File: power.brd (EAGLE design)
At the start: 186 x 186 mm, 126 parts, among them CN2 2X10 HEADER, Q1 IXTK180N15P, Q2 IXTK180N15P, Q4 SPD15P10PL, Q5 2N7002, U1 LT1630, U10 LM2936, U11 LM317, U12 SPST SSR, U2 LT1630, U3 DCDC 15V, U4 DAC80501, U5 DAC80501, U6 ADS1120, U7 LM2662, U8 LM7805, U9 TPS3700

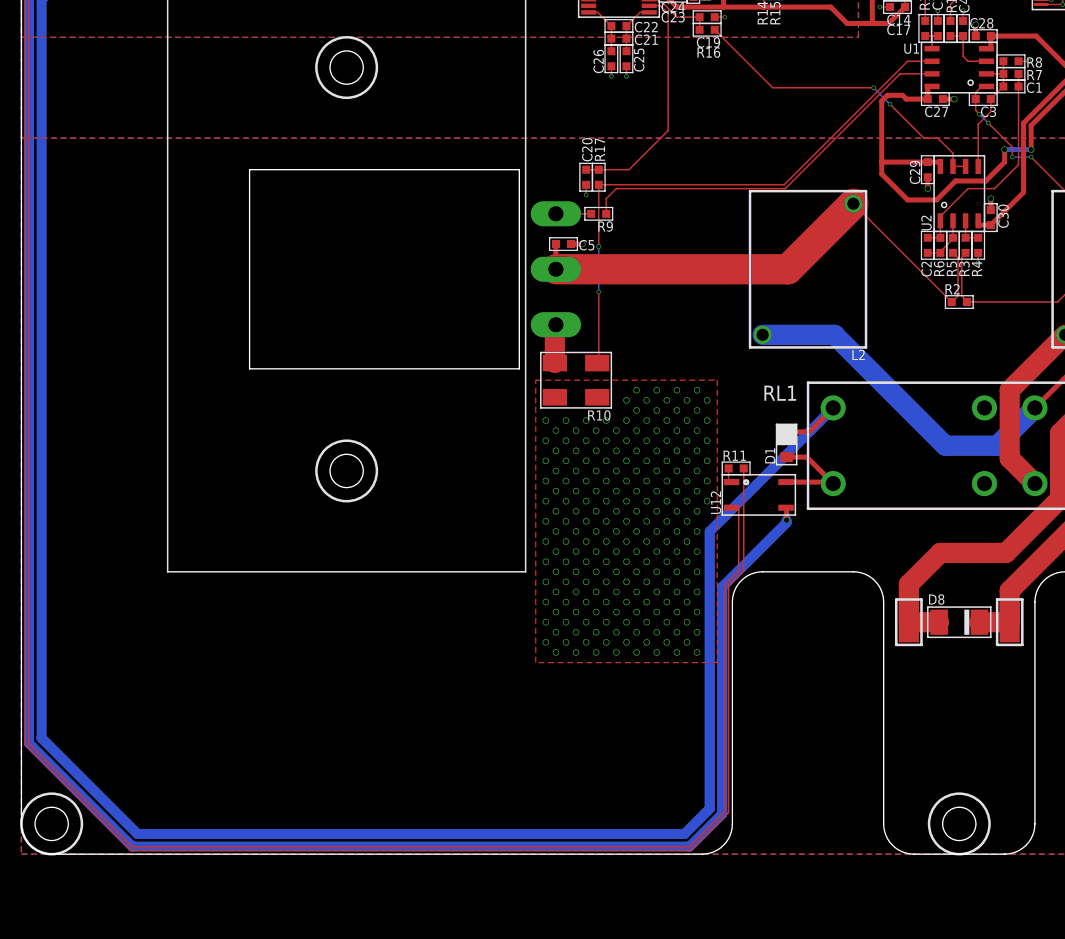
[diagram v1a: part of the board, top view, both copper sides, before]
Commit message: Fixes for stability
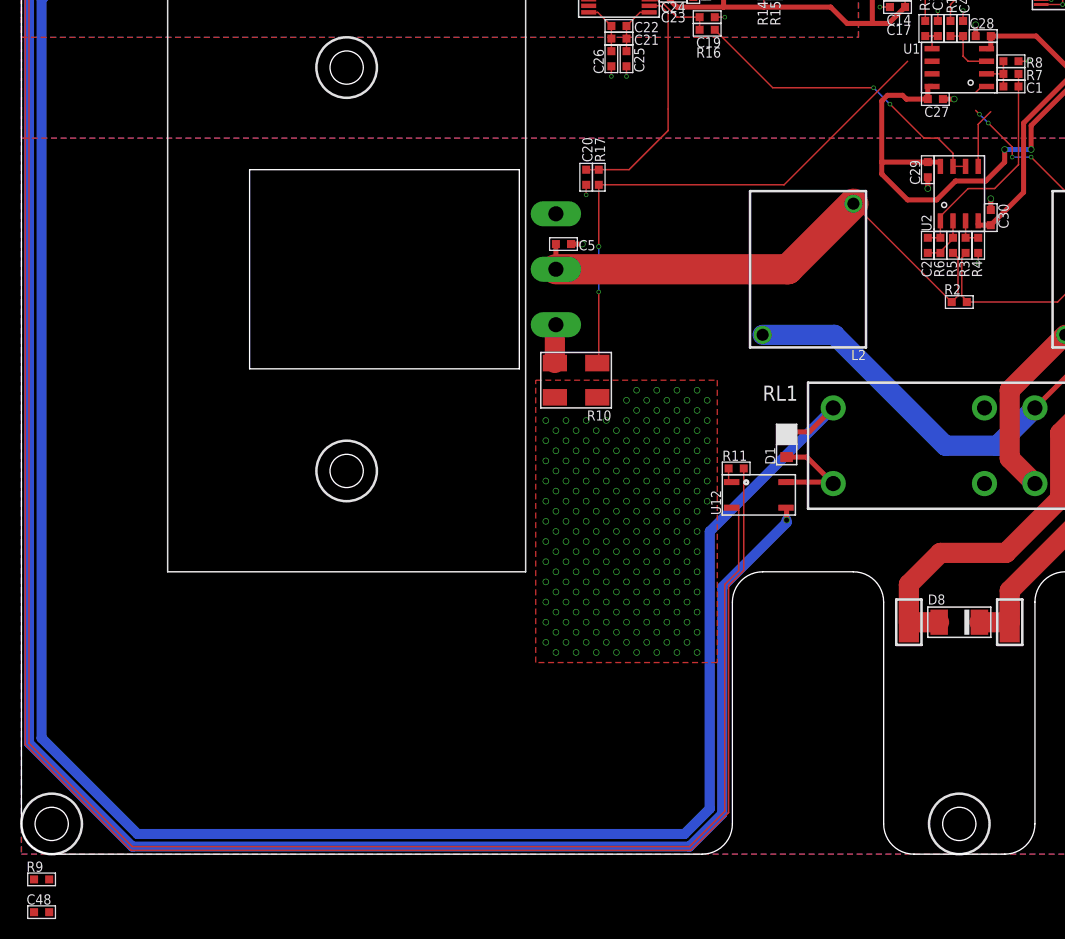
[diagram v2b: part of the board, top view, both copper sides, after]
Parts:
- removed C3: 220pF 50V, CAPACITORS:0603
- added C48: 330pF 50V, CAPACITORS:0603
- C5: value 100nF 16V -> 47nF 16V
- R9: value 10R -> 110R
- moved R9 86.1 mm to (-91.0, -95.5), turned to 0 degrees
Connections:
- net N$1: no longer C3.2
- net N$11: now also C48.1, R9.1, U1.6; no longer Q2.1, R9.2
- net N$345: no longer C3.1
- net N$76: now also R9.2; no longer U1.6
- net N$9: now also C48.2, Q2.1; no longer R9.1
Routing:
- net N$9: track 38.9 -> 0.00 mm
- net N$11: track 3.50 -> 0.00 mm
- net N$345: track 13.1 -> 10.1 mm
- net N$76: track 55.9 -> 53.4 mm
- net N$1: track 45.9 -> 44.1 mm
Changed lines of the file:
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@@
 <attribute name="PRICE_PER" value="0.14" x="89.585" y="16.785" size="1.778" layer="27" rot="R90" display="off"/>
-</element>
-<element name="C3" library="CAPACITORS" package="0603" value="220pF 50V" x="2.375" y="-18.125" smashed="yes" rot="R180">
-<attribute name="DIGIKEY" value="311-1073-1-ND" x="-73.825" y="78.395" size="1.778" layer="27" rot="R180" display="off"/>
-<attribute name="HEIGHT" value="1" x="-73.825" y="78.395" size="1.778" layer="27" rot="R180" display="off"/>
-<attribute name="NAME" x="3.75" y="-18.875" size="1.016" layer="25" rot="R180"/>
-<attribute name="PRICE_PER" value="0.08" x="-73.825" y="78.395" size="1.778" layer="27" rot="R180" display="off"/>
 </element>
 <element name="C30" library="CAPACITORS" package="0603" value="100nF 16V" x="3.125" y="-29.875" smashed="yes" rot="R90">
@@
 <attribute name="PRICE_PER" value="0.08" x="-67.96" y="-53.76" size="1.778" layer="27" rot="R270" display="off"/>
 </element>
-<element name="C5" library="CAPACITORS" package="0603" value="100nF 16V" x="-39.25" y="-32.5" smashed="yes">
-<attribute name="DIGIKEY" value="1276-6582-1-ND" x="44.57" y="-129.02" size="1.778" layer="27" display="off"/>
+<element name="C5" library="CAPACITORS" package="0603" value="47nF 16V" x="-39.25" y="-32.5" smashed="yes">
+<attribute name="DIGIKEY" value="1276-2079-1-ND" x="44.57" y="-129.02" size="1.778" layer="27" display="off"/>
 <attribute name="HEIGHT" value="1" x="44.57" y="-129.02" size="1.778" layer="27" display="off"/>
 <attribute name="NAME" x="-37.75" y="-33.125" size="1.016" layer="25"/>
@@
 <attribute name="NAME" x="6.625" y="-15" size="1.016" layer="25"/>
 <attribute name="PRICE_PER" value="0.10000" x="-40.595" y="85.955" size="1.778" layer="27" rot="R180" display="off"/>
-</element>
-<element name="R9" library="r_0603" package="0603" value="10R" x="-35.75" y="-29.5" smashed="yes" rot="R180">
-<attribute name="DIGIKEY" value="P10.0HCT-ND" x="-85.28" y="70.83" size="1.778" layer="27" rot="R180" display="off"/>
-<attribute name="FARNELL" value="" x="-85.28" y="70.83" size="1.778" layer="27" rot="R180" display="off"/>
-<attribute name="NAME" x="-34.25" y="-30.25" size="1.016" layer="25" rot="R180"/>
-<attribute name="PRICE_PER" value="0.10000" x="-85.28" y="70.83" size="1.778" layer="27" rot="R180" display="off"/>
 </element>
 <element name="RL1" library="ELECTROMECH" package="30MMDPDTRELAY" value="RT424012" x="0" y="-52.5" smashed="yes">
@@
 <attribute name="PRICE_PER" value="0.10000" x="-22.125" y="-54.75" size="1.778" layer="27" rot="R180" display="off"/>
 </element>
+<element name="R9" library="r_0603" package="0603" value="110R" x="-91" y="-95.5" smashed="yes">
+<attribute name="DIGIKEY" value="P110HCT-ND" x="-91" y="-95.5" size="1.778" layer="27" display="off"/>
+<attribute name="FARNELL" value="" x="-91" y="-95.5" size="1.778" layer="27" display="off"/>
+<attribute name="NAME" x="-92.5" y="-94.75" size="1.016" layer="25"/>
+<attribute name="PRICE_PER" value="0.10000" x="-91" y="-95.5" size="1.778" layer="27" display="off"/>
+</element>
+<element name="C48" library="CAPACITORS" package="0603" value="330pF 50V" x="-91" y="-98.75" smashed="yes">
+<attribute name="DIGIKEY" value="311-1075-1-ND" x="-91" y="-98.75" size="1.778" layer="27" display="off"/>
+<attribute name="HEIGHT" value="1" x="-91" y="-98.75" size="1.778" layer="27" display="off"/>
+<attribute name="NAME" x="-92.5" y="-98" size="1.016" layer="25"/>
+<attribute name="PRICE_PER" value="0.1" x="-91" y="-98.75" size="1.778" layer="27" display="off"/>
+</element>
 </elements>
 <signals>
 <signal name="N$1">
 <contactref element="R1" pad="1"/>
-<contactref element="C3" pad="2"/>
 <contactref element="U1" pad="1"/>
 <via x="2" y="-19.625" extent="1-16" drill="0.3"/>
@@
 <wire x1="16" y1="-32.75" x2="23.75" y2="-40.5" width="0.15" layer="1"/>
 <wire x1="23.75" y1="-40.5" x2="35" y2="-40.5" width="0.15" layer="1"/>
-<wire x1="1.625" y1="-18.125" x2="1.625" y2="-19.25" width="0.15" layer="1"/>
 <wire x1="1.625" y1="-19.25" x2="2" y2="-19.625" width="0.15" layer="1"/>
 <wire x1="2.7" y1="-16.875" x2="2.22" y2="-16.875" width="0.15" layer="1"/>
 <wire x1="2.22" y1="-16.875" x2="1.625" y2="-17.47" width="0.15" layer="1"/>
-<wire x1="1.625" y1="-17.47" x2="1.625" y2="-18.125" width="0.15" layer="1"/>
+<wire x1="1.625" y1="-19.25" x2="1.625" y2="-17.47" width="0" layer="19" extent="1-1"/>
 </signal>
 <signal name="N$2">
@@
 <wire x1="-0.875" y1="-11.875" x2="0.375" y2="-11.875" width="0.15" layer="1"/>
 </signal>
-<signal name="N$9">
-<contactref element="R9" pad="1"/>
-<contactref element="U1" pad="7"/>
-<wire x1="-35" y1="-29.5" x2="-35" y2="-28" width="0.15" layer="1"/>
-<wire x1="-34" y1="-27" x2="-35" y2="-28" width="0.15" layer="1"/>
-<wire x1="-17.25" y1="-27" x2="-34" y2="-27" width="0.15" layer="1"/>
-<wire x1="-5.875" y1="-15.625" x2="-2.7" y2="-15.625" width="0.15" layer="1"/>
-<wire x1="-17.25" y1="-27" x2="-5.875" y2="-15.625" width="0.15" layer="1"/>
-</signal>
-<signal name="N$11">
-<contactref element="R9" pad="2"/>
-<contactref element="Q2" pad="1"/>
-<wire x1="-40" y1="-29.5" x2="-36.5" y2="-29.5" width="0.15" layer="1"/>
-</signal>
 <signal name="ADC1_IOUT_SENSE">
 <contactref element="U6" pad="10"/>
@@
 <contactref element="R7" pad="1"/>
 <contactref element="C1" pad="1"/>
-<contactref element="C3" pad="1"/>
 <contactref element="U1" pad="2"/>
 <contactref element="U2" pad="5"/>
@@
 <wire x1="4.375" y1="-14.375" x2="4.375" y2="-15.625" width="0.15" layer="1"/>
 <wire x1="2.7" y1="-15.625" x2="4.375" y2="-15.625" width="0.15" layer="1"/>
-<wire x1="4.375" y1="-16.875" x2="3.125" y2="-18.125" width="0.15" layer="1"/>
-<wire x1="3.125" y1="-18.125" x2="3.125" y2="-19.375" width="0.15" layer="1"/>
 <wire x1="3.125" y1="-19.375" x2="1.875" y2="-20.625" width="0.15" layer="1"/>
+<wire x1="4.375" y1="-16.875" x2="3.125" y2="-19.375" width="0" layer="19" extent="1-1"/>
 </signal>
 <signal name="N$8">
@@
 </signal>
 <signal name="N$76">
-<contactref element="U1" pad="6"/>
 <contactref element="R17" pad="1"/>
 <contactref element="R10" pad="3"/>
-<wire x1="-2.7" y1="-14.375" x2="-5.125" y2="-14.375" width="0.15" layer="1"/>
 <wire x1="-5.125" y1="-14.375" x2="-17.375" y2="-26.625" width="0.15" layer="1"/>
 <via x="-35.75" y="-32.75" extent="1-16" drill="0.35"/>
@@
 <wire x1="-35.75" y1="-44.15" x2="-35.75" y2="-37.25" width="0.15" layer="1"/>
 <wire x1="-35.9" y1="-44.3" x2="-35.75" y2="-44.15" width="0.15" layer="1"/>
+<contactref element="R9" pad="2"/>
+<wire x1="-35.9" y1="-44.3" x2="-90.25" y2="-95.5" width="0" layer="19" extent="1-1"/>
 </signal>
 <signal name="3V3D">
@@
 <wire x1="-22.82" y1="-56.105" x2="-22.57" y2="-56.105" width="0.1524" layer="1"/>
 </signal>
+<signal name="N$9">
+<contactref element="U1" pad="7"/>
+<contactref element="Q2" pad="1"/>
+<contactref element="C48" pad="2"/>
+<wire x1="-40" y1="-29.5" x2="-90.25" y2="-98.75" width="0" layer="19" extent="1-1"/>
+<wire x1="-2.7" y1="-15.625" x2="-40" y2="-29.5" width="0" layer="19" extent="1-1"/>
+</signal>
+<signal name="N$11">
+<contactref element="U1" pad="6"/>
+<contactref element="R9" pad="1"/>
+<contactref element="C48" pad="1"/>
+<wire x1="-91.75" y1="-95.5" x2="-91.75" y2="-98.75" width="0" layer="19" extent="1-1"/>
+<wire x1="-2.7" y1="-14.375" x2="-91.75" y2="-95.5" width="0" layer="19" extent="1-1"/>
+</signal>
 </signals>
